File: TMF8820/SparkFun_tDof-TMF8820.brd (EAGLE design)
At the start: 25.4 x 25.4 mm, 53 parts, among them J4 QWIIC_RIGHT_ANGLE, J5 QWIIC_RIGHT_ANGLE

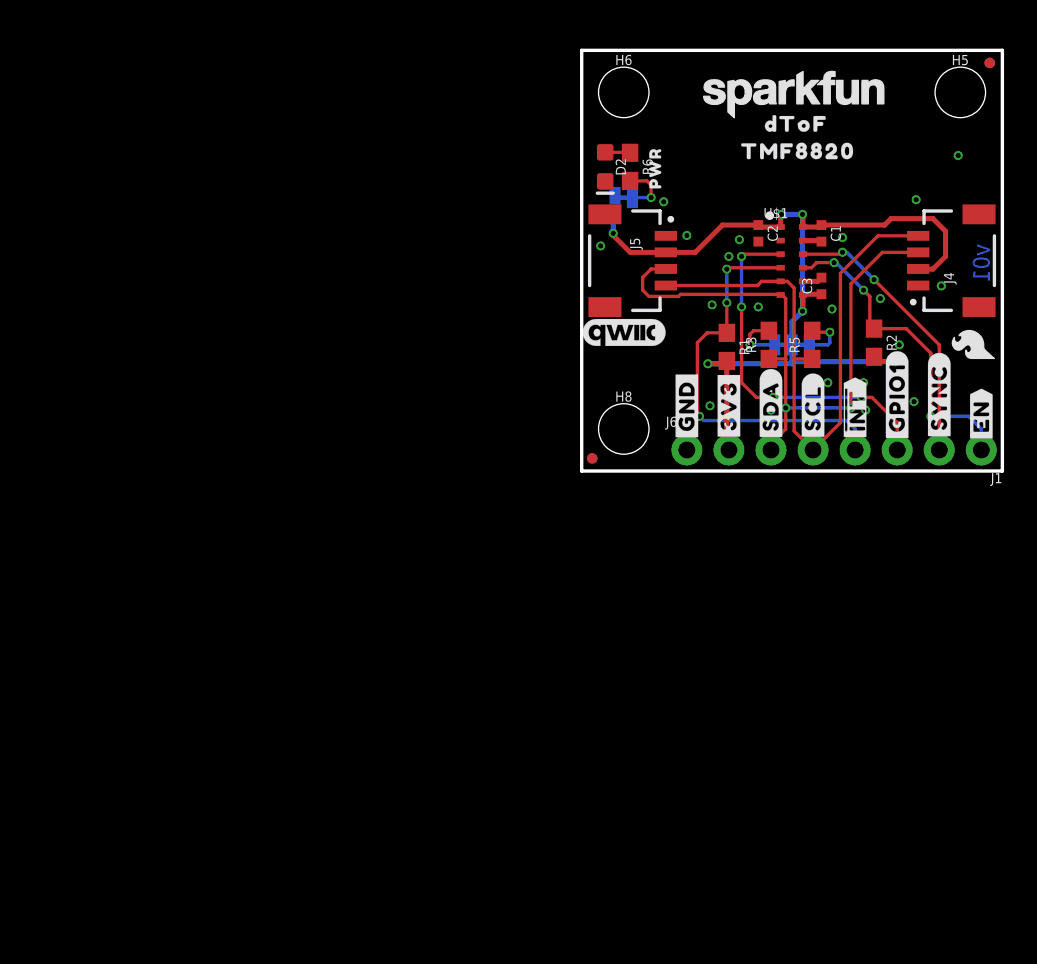
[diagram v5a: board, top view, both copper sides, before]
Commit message: Updates the TMF882X device in the library to have two variants of the two ICs
* Better silk labeling for the 8820 and 8820 HQ
* Adds new IC variants to both designs
* Adds default addresses to schematics
* Moves some traces and vias for better ground pour in the 8820 design
* Moves entire 8820 design to origin in board file
* Adds measure from center of qwiic connector to edge in 8820 design
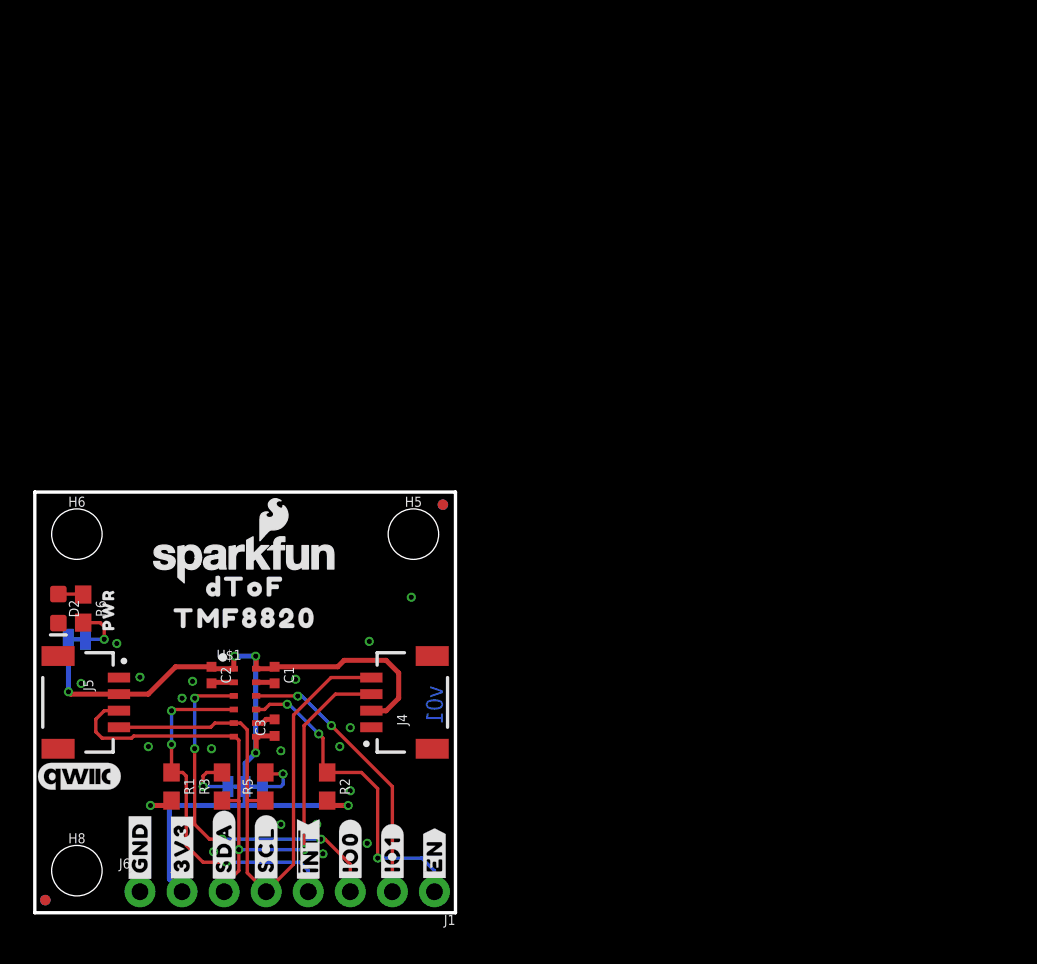
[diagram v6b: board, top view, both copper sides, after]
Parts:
- removed U$25: (no value), SparkFun-Aesthetics:SFE_LOGO_FLAME_.1
- added U$8: (no value), TMFTopSilk:#IO0#8
- added U$9: (no value), TMFTopSilk:#IO1#8
- U$1: value TMF8820- -> TMF882X_TMF8820
- U$10: device TMFTopSilk:##INT##8 -> TMFBotSilk:##INT##9
- U$11: device TMFTopSilk:TMF88209 -> TMFTopSilk:DTOF882188211
- U$12: device TMFTopSilk:DTOF882188211 -> TMFTopSilk:TMF88209
- U$13: device SparkFun-Aesthetics:SFE_LOGO_NAME_.1 -> SparkFun-Aesthetics:SFE_LOGO_NAME_FLAME_.1
- U$15: device TMFBotSilk:##INT##9 -> TMFBotSilk:#SYNC#8
- U$19: device TMFBotSilk:#GPIO1#8 -> TMFTopSilk:#IO0#8
- U$24: device TMFBotSilk:#SYNC#8 -> TMFTopSilk:##INT##8
- U$26: device TMFTopSilk:TMF882021 -> TMFTopSilk:DTOF882188211
- U$27: device TMFTopSilk:DTOF8821882023 -> TMFTopSilk:TMF88209
- moved U$30 49.6 mm to (8.51, 11.6)
- moved U$24 46.9 mm to (16.5, 3.68), flipped to the bottom, turned to 270 degrees
- moved U$29 45.5 mm to (12.3, 11.7)
- moved U$28 45.1 mm to (16.1, 11.7)
- moved U$12 44.7 mm to (12.7, 17.8)
- moved U$13 43.4 mm to (12.7, 21.3)
- moved U$19 42.9 mm to (19.1, 3.68), flipped to the bottom
- moved R1 42.8 mm to (8.26, 7.62)
- moved R2 42.5 mm to (17.7, 7.62)
- moved U$11 42.5 mm to (12.7, 19.7)
- moved C1 42.4 mm to (14.5, 14.4)
- moved C2 42.4 mm to (10.7, 14.4)
- moved FD5 42.4 mm to (0.64, 0.76)
- moved FD8 42.4 mm to (0.64, 0.76)
- moved FRAME2 42.4 mm to (-11.9, -16.8)
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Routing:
- net !INT!: track 24.6 -> 22.0 mm
- net GND: track 2.35 -> 3.72 mm, vias 21 -> 20
- net 3.3V: track 59.8 -> 61.1 mm
